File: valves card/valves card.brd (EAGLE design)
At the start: 100 x 80 mm, 68 parts, among them J1 09231486921, J2 TBP02R1-381-14BE, Q1 IRLZ44NSTRLPBF, Q11 IRLZ44NSTRLPBF, Q13 IRLZ44NSTRLPBF, Q15 IRLZ44NSTRLPBF, Q17 IRLZ44NSTRLPBF, Q19 IRLZ44NSTRLPBF, Q21 IRLZ44NSTRLPBF, Q23 IRLZ44NSTRLPBF, Q3 IRLZ44NSTRLPBF, Q5 IRLZ44NSTRLPBF, Q7 IRLZ44NSTRLPBF, Q9 IRLZ44NSTRLPBF, U1 LM2937IMP-10, U10 OR-815, U12 OR-815, U14 OR-815, U16 OR-815, U18 OR-815, U2 EL817(D)-ND, U20 OR-815, U22 OR-815, U24 OR-815, U4 OR-815, U6 OR-815, U8 OR-815

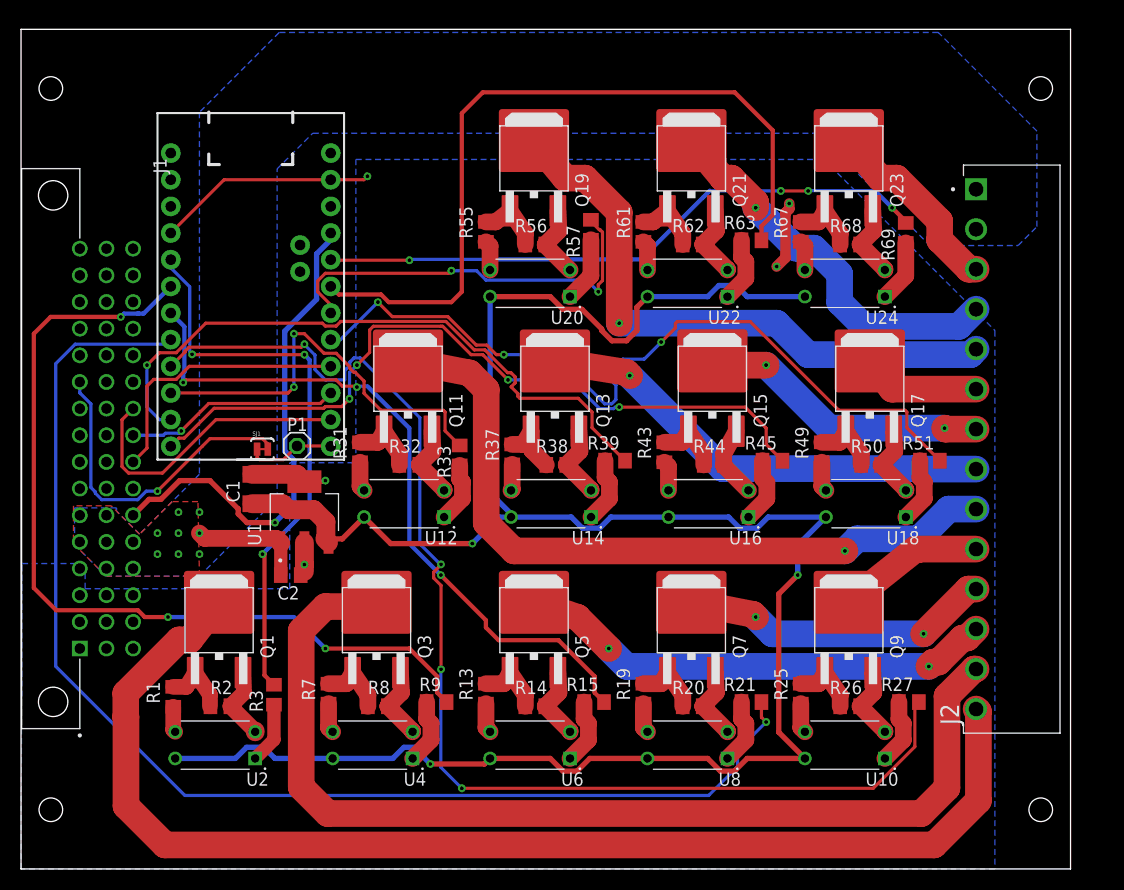
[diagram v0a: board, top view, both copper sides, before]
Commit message: cleaned up valves board silkscreen, moved header forwards
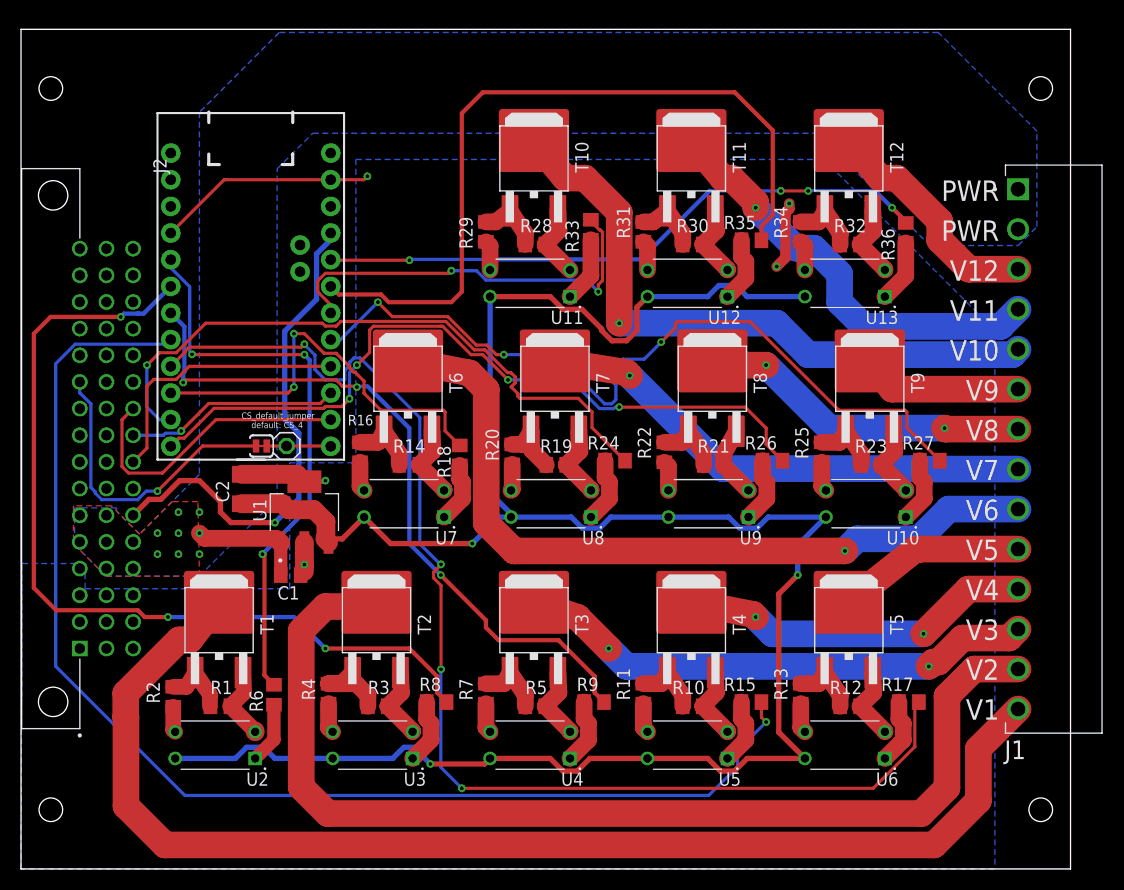
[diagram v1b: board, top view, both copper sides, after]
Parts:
- removed P1: (no value), pinhead:1X01
- removed R37, R49, R61: 600, eagle-ltspice:R0805
- removed R38, R44, R68: 10k, eagle-ltspice:R0805
- removed R45, R51, R57: 100, eagle-ltspice:R0805
- removed U14, U18, U22: OR-815, EL817C:DIP762W25P254L650H453Q4B
- added JP1: (no value), pinhead:1X01
- added R10, R12, R5: 10k, eagle-ltspice:R0805
- added R11, R16, R4: 600, eagle-ltspice:R0805
- added R17, R18, R6: 100, eagle-ltspice:R0805
- added U3, U5, U7: EL817(D)-ND, EL817C:DIP762W25P254L650H453Q4B
- C1: value 10Uf -> 0.1Uf; device eagle-ltspice:C1206 -> eagle-ltspice:C0805
- C2: value 0.1Uf -> 10Uf; device eagle-ltspice:C0805 -> eagle-ltspice:C1206
- J1: value 09231486921 -> TBP02R1-381-14BE; device din41612_48_pin_board:HARTING_09231486921 -> TBP02R1-381-14BE:CUI_TBP02R1-381-14BE
- J2: value TBP02R1-381-14BE -> 09231486921; device TBP02R1-381-14BE:CUI_TBP02R1-381-14BE -> din41612_48_pin_board:HARTING_09231486921
- M1: value (none) -> SAM_D21_MINI_BREAKOUT
- R1, R19: value 600 -> 10k
- R2, R20: value 10k -> 600
- R21, R3: value 100 -> 10k
- R26, R8: value 10k -> 100
- U1: value LM2937IMP-10 -> LM2937IMP-12
- U10, U11, U12, U13, U4, U6, U8, U9: value OR-815 -> EL817(D)-ND
- moved J1 99.5 mm to (95.0, 64.8)
- moved J2 96.0 mm to (5.60, 21.0)
- moved R32 47.0 mm to (79.0, 59.5)
- moved R31 34.2 mm to (59.3, 60.7)
- moved U12 34.2 mm to (63.5, 55.8)
- moved R13 30.0 mm to (74.3, 16.7)
- moved U6 30.0 mm to (78.5, 11.8)
- moved R20 29.5 mm to (46.8, 39.5), turned to 90 degrees
- moved U8 26.4 mm to (50.5, 34.8)
- moved R14 25.9 mm to (37.0, 38.5)
- moved R33 24.9 mm to (54.3, 60.9)
- moved R26 24.5 mm to (71.6, 38.9)
- moved R19 23.3 mm to (51.0, 38.5), turned to 180 degrees
- moved R25 23.1 mm to (76.3, 39.7)
- moved R27 23.1 mm to (86.6, 38.9)
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- renumbered Q1 to T1, Q11 to T6, Q13 to T7, Q15 to T8, Q17 to T9, Q19 to T10, Q21 to T11, Q23 to T12, Q3 to T2, Q5 to T3, Q7 to T4, Q9 to T5, R39 to R24, R43 to R22, R50 to R23, R55 to R29, R56 to R28, R62 to R30, R63 to R35, R67 to R34, R69 to R36, U$1 to M1, U16 to U9, U20 to U11, U24 to U13
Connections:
- removed net N$23 (its old number): R15.2, U6.1
- removed net N$58 (its old number): R49.1, U18.3
- removed net N$59 (its old number): R51.2, U18.1
- removed net N$70 (its old number): R61.1, U22.3
- new net N$16: R4.1, U3.3
- new net N$17: R8.2, U3.1
- new net N$35: R17.2, U6.1
- new net N$40: R16.1, U7.3
- net 12V: now also C2.1, U3.4, U5.4, U7.4; no longer C1.1, U14.4, U18.4, U22.4
- net 24V: now also C1.1, J1.1, J1.2, J2.20, J2.21, J2.22, J2.36, J2.37, J2.5, J2.6; no longer C2.1, J1.20, J1.21, J1.22, J1.36, J1.37, J1.5, J1.6, J2.1, J2.2
- net 3.3V: now also J2.38; no longer J1.38
- net 5V: now also J2.23, J2.39; no longer J1.23, J1.39
- net DRAIN1: now also J1.14; no longer J2.14
- net DRAIN10: now also J1.5; no longer J2.5
- net DRAIN11: now also J1.4; no longer J2.4
- net DRAIN12: now also J1.3; no longer J2.3
- net DRAIN2: now also J1.13; no longer J2.13
- net DRAIN3: now also J1.12; no longer J2.12
- net DRAIN4: now also J1.11; no longer J2.11
- net DRAIN5: now also J1.10; no longer J2.10
- net DRAIN6: now also J1.9; no longer J2.9
- net DRAIN7: now also J1.8; no longer J2.8
- net DRAIN8: now also J1.7; no longer J2.7
- net DRAIN9: now also J1.6; no longer J2.6
- net EXT_1: now also J2.15; no longer J1.15
- net EXT_2: now also J2.16; no longer J1.16
- net EXT_3: now also J2.31; no longer J1.31
- net EXT_4: now also J2.32; no longer J1.32
- net EXT_5: now also J2.46; no longer J1.46
- net EXT_6: now also J2.47; no longer J1.47
- net EXT_7: now also J2.48; no longer J1.48
- net GND: now also J2.1, J2.17, J2.18, J2.19, J2.2, J2.3, J2.33, J2.34, J2.35, J2.4, R1.1, R10.1, R12.1, R19.1, R21.1, R3.1, R5.1, U3.2, U5.2, U7.2; no longer J1.1, J1.17, J1.18, J1.19, J1.2, J1.3, J1.33, J1.34, J1.35, J1.4, R2.1, R20.1, R26.1, R38.1, R44.1, R68.1, R8.1, U14.2, U18.2, U22.2
- net MISO: now also J2.41; no longer J1.41
- net MOSI: now also J2.42; no longer J1.42
- net N$11: now also R2.1; no longer R1.1
- net N$15: now also R3.2, R4.2; no longer R7.2, R8.2
- net N$2: now also JP1.1; no longer P1.1
- net N$21: now also R5.2, R7.2; no longer R13.2, R14.2
- net N$27: now also R10.2, R11.2; no longer R19.2, R20.2
- net N$28: now also R11.1, U5.3; no longer R19.1, U8.3
- net N$29: now also R15.2, U5.1; no longer R21.2, U8.1
- net N$33: now also R12.2, R13.2; no longer R25.2, R26.2
- net N$39: now also R14.2, R16.2; no longer R31.2, R32.2
- net N$41: now also R18.2, U7.1; no longer R33.2, U12.1
- net N$45: now also R19.2, R20.2; no longer R37.2, R38.2
- net N$46: now also R20.1, U8.3; no longer R37.1, U14.3
- net N$47: now also U8.1; no longer U14.1
- net N$5: now also R6.2; no longer R3.2
- net N$51: now also R21.2; no longer R44.2
- net N$53: now also R26.2; no longer R45.2
- net N$57: now also R25.2; no longer R49.2
- net N$65: now also R33.2; no longer R57.2
- net N$69: now also R31.2; no longer R61.2
- net N$71: now also U12.1; no longer U22.1
- net N$75: now also R32.2; no longer R68.2
- net SCK: now also J2.40; no longer J1.40
- net SCL: now also J2.44; no longer J1.44
- net SDA: now also J2.43; no longer J1.43
- net SOL1: now also R6.1; no longer R3.1
- net SOL10: now also R33.1; no longer R57.1
- net SOL2: now also R8.1; no longer R9.1
- net SOL3: now also R9.1; no longer R15.1
- net SOL4: now also R15.1; no longer R21.1
- net SOL5: now also R17.1; no longer R27.1
- net SOL6: now also R18.1; no longer R33.1
- net SOL8: now also R26.1; no longer R45.1
- net SOL9: now also R27.1; no longer R51.1
- net SS_1: now also J2.8; no longer J1.8
- net SS_10: now also J2.26; no longer J1.26
- net SS_11: now also J2.27; no longer J1.27
- net SS_12: now also J2.28; no longer J1.28
- net SS_13: now also J2.29; no longer J1.29
- net SS_14: now also J2.30; no longer J1.30
- net SS_15: now also J2.45; no longer J1.45
- net SS_2: now also J2.9; no longer J1.9
- net SS_3: now also J2.10; no longer J1.10
- net SS_4: now also J2.11; no longer J1.11
- net SS_5: now also J2.12; no longer J1.12
- net SS_6: now also J2.13; no longer J1.13
- net SS_7: now also J2.14; no longer J1.14
- net SS_8: now also J2.24; no longer J1.24
- net SS_9: now also J2.25; no longer J1.25
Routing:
- net N$23 (its old number): track 6.27 -> 0.00 mm
- net N$17: track 0.00 -> 6.27 mm
- net N$35: track 0.00 -> 6.27 mm
- net N$59 (its old number): track 6.27 -> 0.00 mm
- net DRAIN4: track 32.1 -> 36.1 mm
- net DRAIN9: track 11.4 -> 15.4 mm
- net DRAIN8: track 27.9 -> 31.9 mm
- net DRAIN7: track 44.0 -> 48.0 mm
- net DRAIN6: track 71.6 -> 75.6 mm
- net DRAIN3: track 45.8 -> 49.8 mm
- net DRAIN2: track 99.5 -> 103.5 mm
- net DRAIN12: track 18.5 -> 22.5 mm
- net DRAIN11: track 37.2 -> 41.2 mm
- net DRAIN10: track 57.2 -> 61.2 mm
- net DRAIN5: track 13.9 -> 17.9 mm
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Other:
- board text added: "CS_default_jumper default: CS_4"
- board text added: "PWR PWR V12 V11 V10 V9 V8 V7 V6 V5 V4 V3 V2 V1"

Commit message: improved silkscreen for valve board
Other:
- board text added: "MICRO 1"
- board text added: "PolyVent Motor Card V2.1 Public invention - CERN OHL 2.0"
- board text added: "Serial Number:"
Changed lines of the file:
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@@
 V2
 V1</text>
+<rectangle x1="82.61" y1="66.89" x2="86.61" y2="83.89" layer="25" rot="R90"/>
+<text x="92.6" y="79.91" size="1.778" layer="25" rot="R180">Serial Number:</text>
+<text x="37.57" y="73.43" size="1.778" layer="25">PolyVent Motor Card V2.1
+Public invention - CERN OHL 2.0</text>
+<text x="22" y="53" size="1.778" layer="25" rot="R90">MICRO 1</text>
 </plain>
 <attributes>

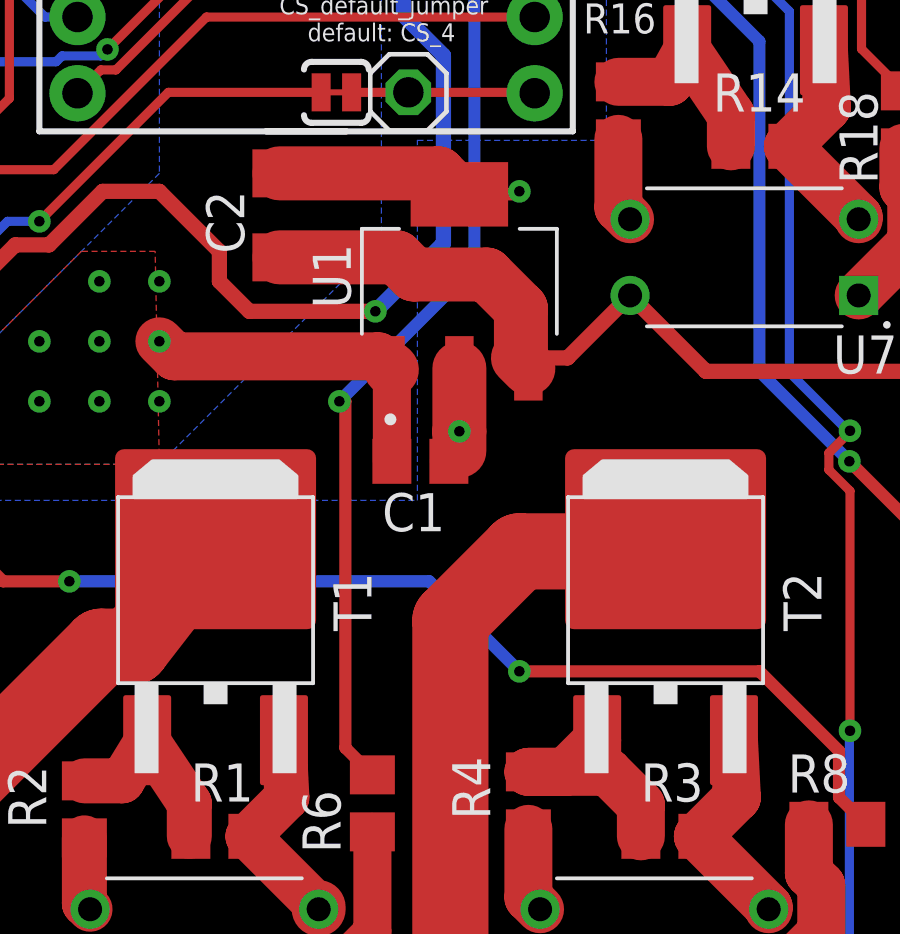
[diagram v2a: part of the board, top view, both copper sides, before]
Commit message: cleaned up sensor board silkscreen + added test pads
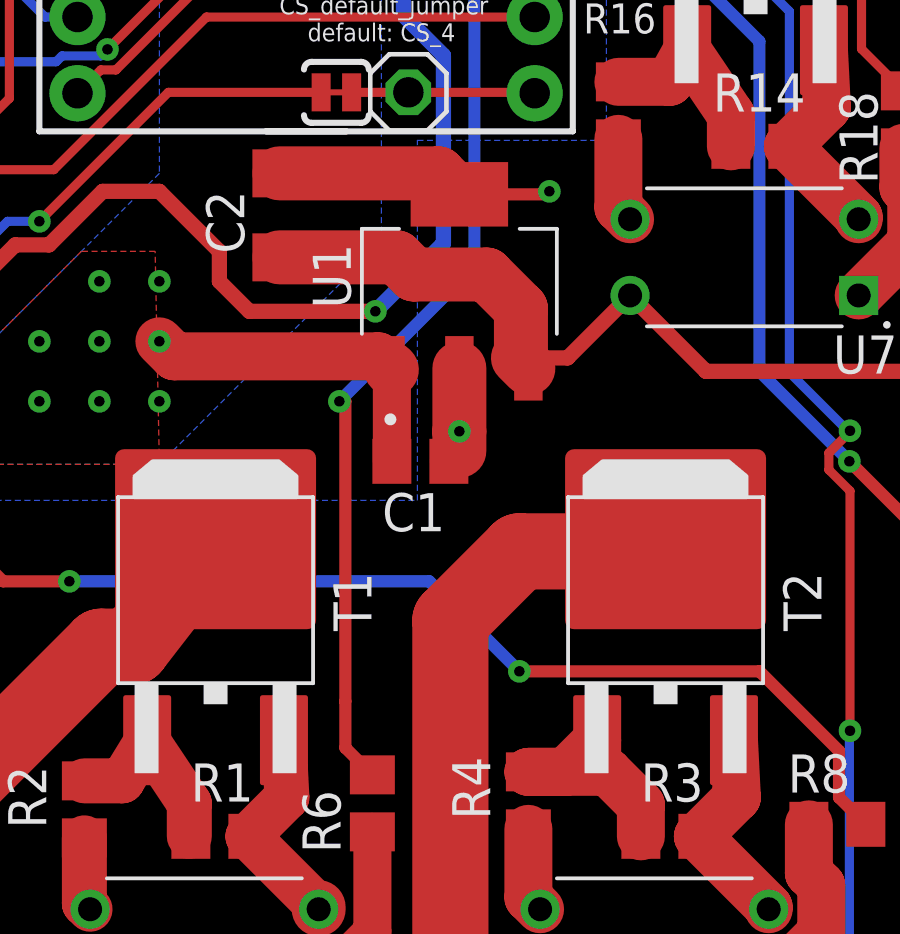
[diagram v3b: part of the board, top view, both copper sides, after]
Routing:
- net GND: track 124.7 -> 125.7 mm
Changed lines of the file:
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@@
 </polygon>
 <via x="27" y="29" extent="1-16" drill="0.35"/>
-<wire x1="27" y1="36.9" x2="28.9" y2="36.9" width="0.4064" layer="1"/>
-<wire x1="28.9" y1="36.9" x2="29" y2="37" width="0.4064" layer="1"/>
-<via x="29" y="37" extent="1-16" drill="0.35"/>
+<wire x1="27" y1="36.9" x2="29.9" y2="36.9" width="0.4064" layer="1"/>
+<wire x1="29.9" y1="36.9" x2="30" y2="37" width="0.4064" layer="1"/>
+<via x="30" y="37" extent="1-16" drill="0.35"/>
 <via x="72" y="57.4" extent="1-16" drill="0.35"/>
 <via x="73.2" y="63.4" extent="1-16" drill="0.35"/>
@@
 <contactref element="M1" pad="8@JP1"/>
 <wire x1="24.1" y1="17.55" x2="23.2" y2="18.45" width="0.4064" layer="1"/>
-<wire x1="23.2" y1="18.45" x2="23.2" y2="30" width="0.4064" layer="1"/>
+<wire x1="23.2" y1="18.45" x2="23.2" y2="20" width="0.4064" layer="1"/>
+<wire x1="23.2" y1="20" x2="23.2" y2="30" width="0.4064" layer="1"/>
 <wire x1="23.2" y1="30" x2="23" y2="30" width="0.4064" layer="1"/>
 <via x="23" y="30" extent="1-16" drill="0.35"/>

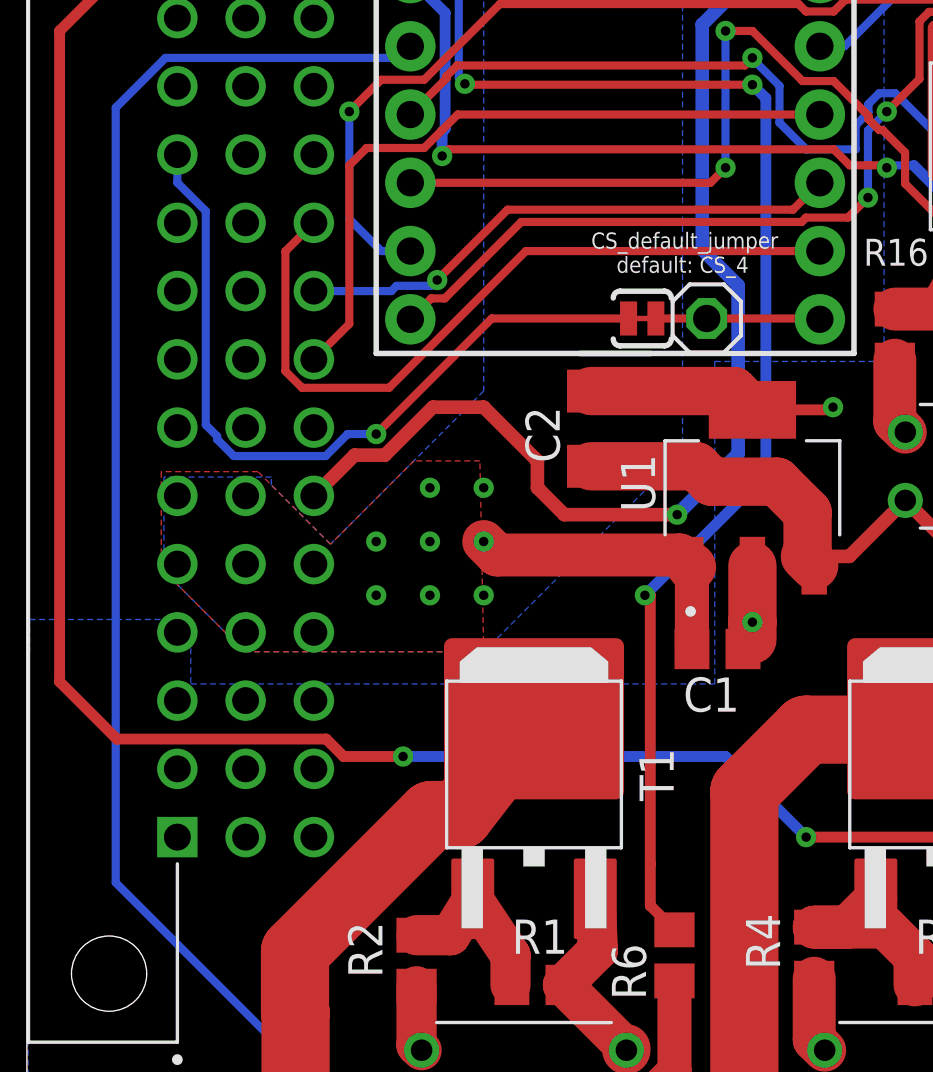
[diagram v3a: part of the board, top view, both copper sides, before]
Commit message: changed pinouts for the boards, next I have to make accomodations for new pinouts and the USB selector system
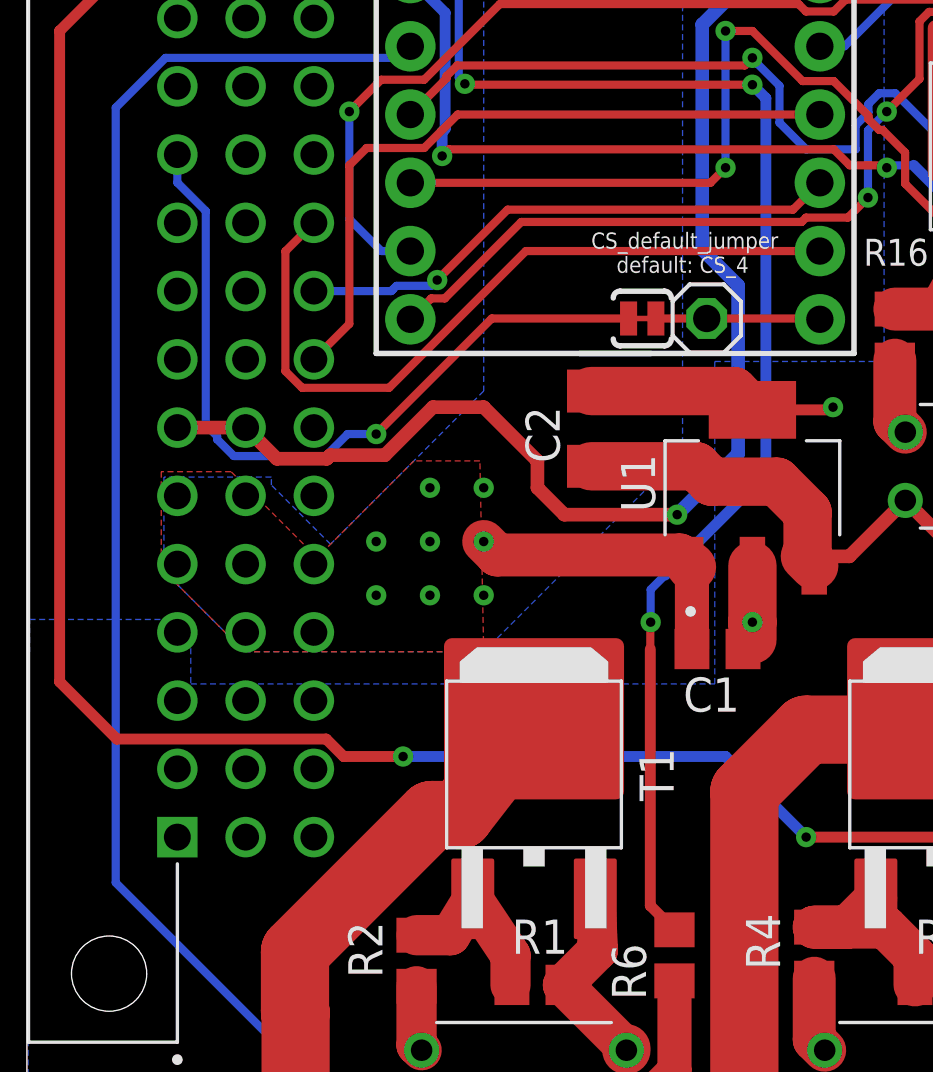
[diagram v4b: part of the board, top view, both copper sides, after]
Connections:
- net 24V renamed 24V/12V
- net EXT_1 renamed USB1_D-
- net EXT_2 renamed USB1_D+
- net EXT_3 renamed USB2_D-
- net EXT_4 renamed USB2_D+
- net EXT_5 renamed USB3_D-
- net EXT_6 renamed USB3_D+
- net SS_1 renamed CS_1
- net SS_10 renamed CS_10
- net SS_11 renamed CS_11
- net SS_12 renamed CS_12
- net SS_13 renamed CS_13
- net SS_14 renamed CS_14
- net SS_15 renamed CS_15
- net SS_2 renamed CS_2
- net SS_3 renamed CS_3
- net SS_4 renamed CS_4
- net SS_5 renamed CS_5
- net SS_6 renamed CS_6
- net SS_7 renamed CS_7
- net SS_8 renamed CS_8
- net SS_9 renamed CS_9
- removed net EXT_7: J2.48
- new net RESET: J2.48, M1.10@JP1
- net 3.3V: now also J2.23, J2.7; no longer J2.38
- net 5V: now also J2.38; no longer J2.23
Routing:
- net 3.3V: track 48.0 -> 53.0 mm
